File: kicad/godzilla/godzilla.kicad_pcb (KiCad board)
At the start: 2 copper layers, 3 parts, among them U1 NE555P

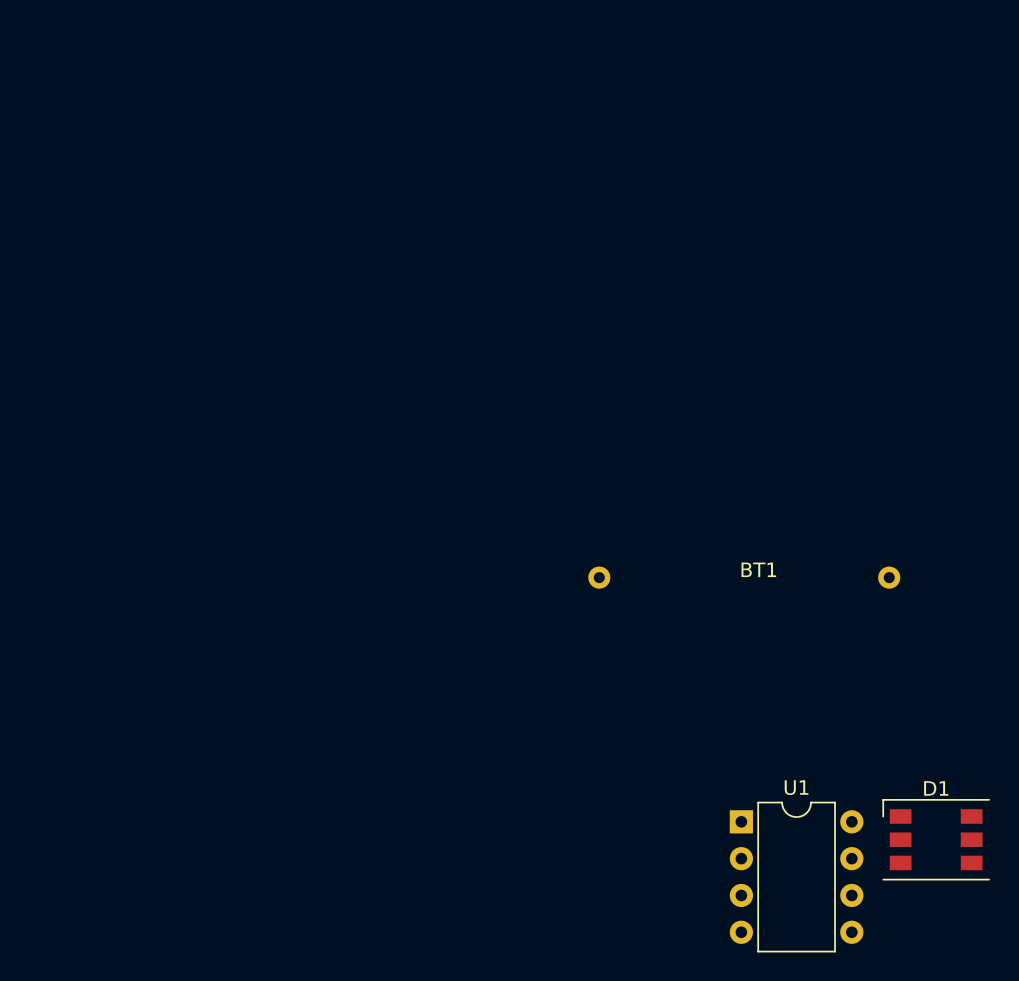
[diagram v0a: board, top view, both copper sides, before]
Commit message: Fixed vector timing for stupid DACs
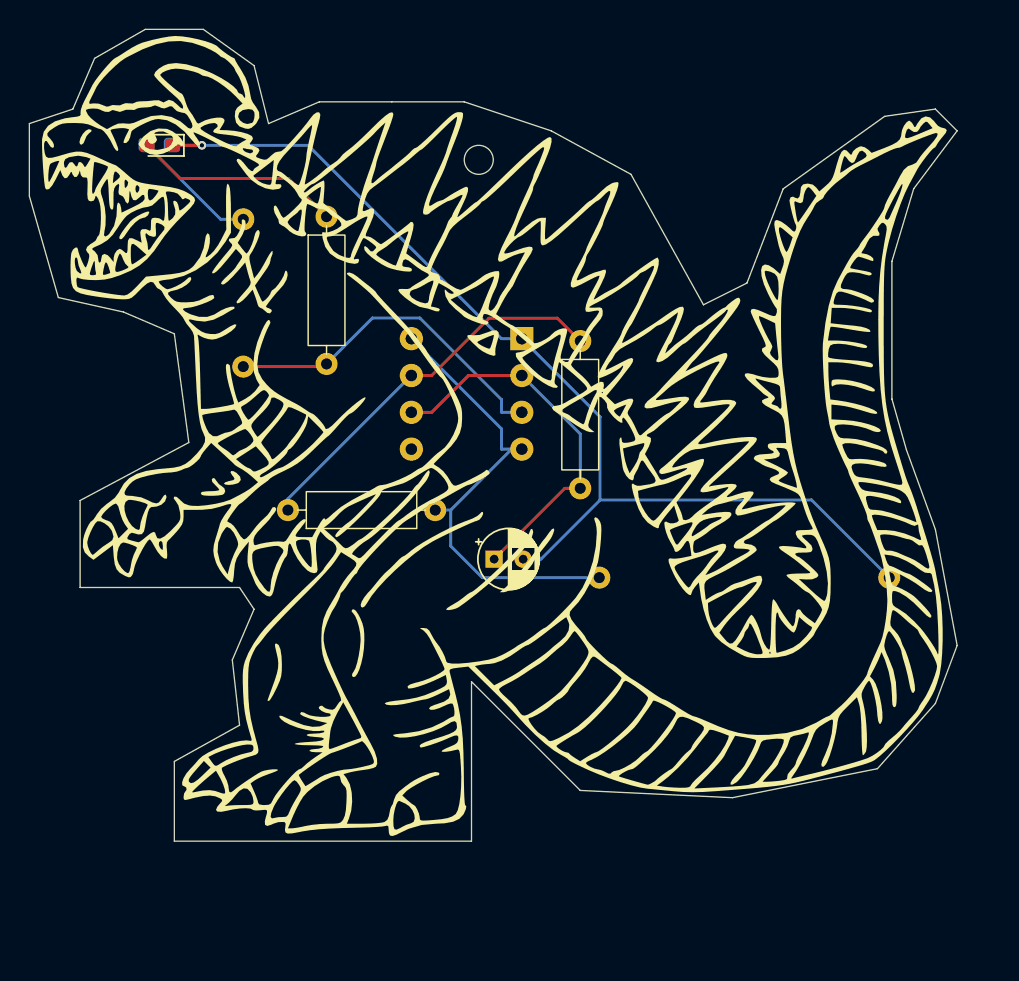
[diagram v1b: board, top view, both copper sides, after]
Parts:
- added C1: C, Capacitor_THT:CP_Radial_D4.0mm_P2.00mm, F.Cu at (124.1, 82.5)
- added D2: LED, LED_SMD:LED_0603_1608Metric_Pad1.05x0.95mm_HandSolder, F.Cu at (101.0, 54.0)
- added R1: R, custom_footprint_library:0.4_pitch_resistor, F.Cu at (114.9, 79.2)
- added R2: R, custom_footprint_library:0.4_pitch_resistor, F.Cu at (130.0, 72.6)
- added R3: R, custom_footprint_library:0.4_pitch_resistor, B.Cu at (106.8, 64.2)
- added R4: R, custom_footprint_library:0.4_pitch_resistor, F.Cu at (112.5, 64.0)
- added U2: ~, custom_footprint_library:godzilla_silkscreen, F.Cu at (121.5, 69.5)
- D1: value LED_RGB -> LED; footprint LED_SMD:LED_WS2812_PLCC6_5.0x5.0mm_P1.6mm -> LED_SMD:LED_0603_1608Metric_Pad1.05x0.95mm_HandSolder; moved to B.Cu
- U1: moved to B.Cu
- moved D1 71.9 mm to (100.9, 54.0), turned to 180 degrees
- moved U1 36.6 mm to (126.0, 67.3), turned to 180 degrees
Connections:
- BT1 pad 1: unconnected-(BT1-+-Pad1) -> Net-(BT1-+)
- BT1 pad 2: unconnected-(BT1---Pad2) -> Net-(BT1--)
- D1 pad 1: unconnected-(D1-RK-Pad1) -> Net-(BT1--)
- D1 pad 2: unconnected-(D1-GK-Pad2) -> Net-(D1-A)
- U1 pad 1: unconnected-(U1-GND-Pad1) -> Net-(BT1--)
- U1 pad 2: unconnected-(U1-TR-Pad2) -> Net-(U1-THR)
- U1 pad 3: unconnected-(U1-Q-Pad3) -> Net-(U1-Q)
- U1 pad 4: unconnected-(U1-R-Pad4) -> Net-(BT1-+)
- U1 pad 6: unconnected-(U1-THR-Pad6) -> Net-(U1-THR)
- U1 pad 7: unconnected-(U1-DIS-Pad7) -> Net-(U1-DIS)
- U1 pad 8: unconnected-(U1-VCC-Pad8) -> Net-(BT1-+)
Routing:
- net Net-(BT1--): track 0.00 -> 74.3 mm, vias 0 -> 1
- net Net-(BT1-+): track 0.00 -> 32.2 mm
- net Net-(U1-DIS): track 0.00 -> 26.8 mm
- net Net-(U1-THR): track 0.00 -> 26.1 mm
- net Net-(U1-Q): track 0.00 -> 23.8 mm
- net Net-(D2-A): track 0.00 -> 14.4 mm
- net Net-(D1-A): track 0.00 -> 8.83 mm
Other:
- board outline added: 64 x 56 mm
